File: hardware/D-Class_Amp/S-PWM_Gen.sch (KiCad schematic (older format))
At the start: 13 parts, among them U201 Opamp_Dual_Generic, U202 Comparator_Dual_Generic

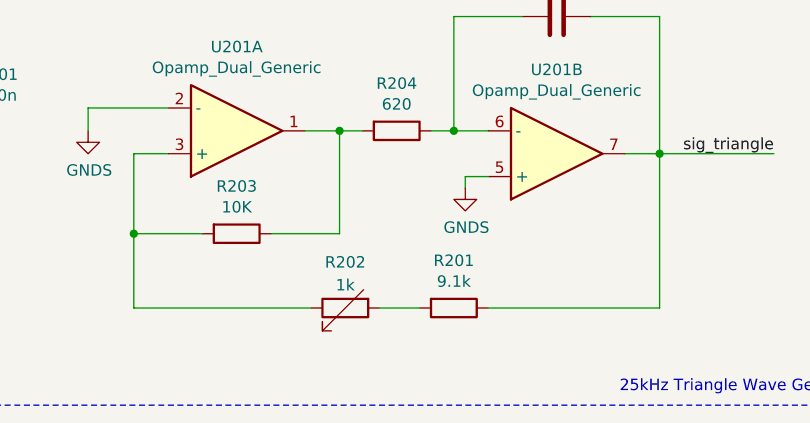
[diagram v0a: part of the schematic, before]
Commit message: update potentiometer, add footprints
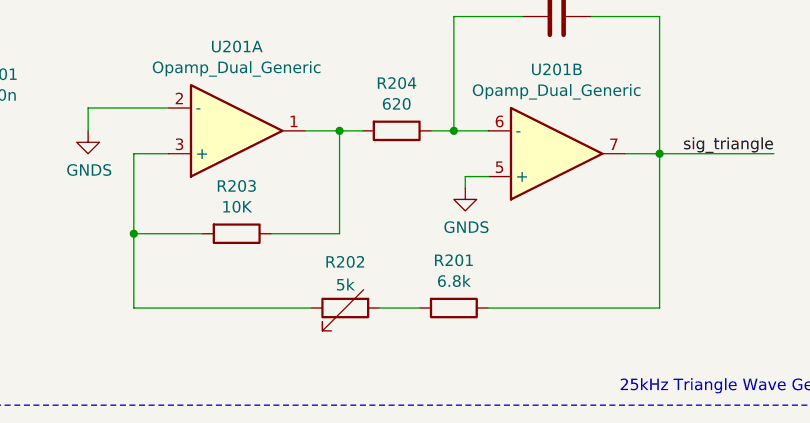
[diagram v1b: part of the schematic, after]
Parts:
- C201, C202, C203, C204, C205, R203, R204, R205, R206: footprint (none) -> Resistor_SMD:R_0805_2012Metric_Pad1.20x1.40mm_HandSolder
- R201: value 9.1k -> 6.8k; footprint (none) -> Resistor_SMD:R_0805_2012Metric_Pad1.20x1.40mm_HandSolder
- R202: value 1k -> 5k; footprint (none) -> Potentiometer_THT:Potentiometer_Vishay_T73YP_Vertical
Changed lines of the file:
@@
 F 0 "C203" V 4123 1325 50  0000 C CNN
 F 1 "15n 16V" V 4214 1325 50  0000 C CNN
-F 2 "" H 4413 1175 50  0001 C CNN
+F 2 "Resistor_SMD:R_0805_2012Metric_Pad1.20x1.40mm_HandSolder" H 4413 1175 50  0001 C CNN
 F 3 "~" H 4375 1325 50  0001 C CNN
 	1    4375 1325
@@
 F 0 "R203" V 2768 2275 50  0000 C CNN
 F 1 "10K" V 2859 2275 50  0000 C CNN
-F 2 "" V 2905 2275 50  0001 C CNN
+F 2 "Resistor_SMD:R_0805_2012Metric_Pad1.20x1.40mm_HandSolder" V 2905 2275 50  0001 C CNN
 F 3 "~" H 2975 2275 50  0001 C CNN
 	1    2975 2275
@@
 F 0 "R204" V 3468 1825 50  0000 C CNN
 F 1 "620" V 3559 1825 50  0000 C CNN
-F 2 "" V 3605 1825 50  0001 C CNN
+F 2 "Resistor_SMD:R_0805_2012Metric_Pad1.20x1.40mm_HandSolder" V 3605 1825 50  0001 C CNN
 F 3 "~" H 3675 1825 50  0001 C CNN
 	1    3675 1825
@@
 	4675 1925 4825 1925
 $Comp
-L power:GNDS #PWR?
+L power:GNDS #PWR0122
 U 1 1 61064912
 P 2325 1825
-F 0 "#PWR?" H 2325 1575 50  0001 C CNN
+F 0 "#PWR0122" H 2325 1575 50  0001 C CNN
 F 1 "GNDS" H 2330 1652 50  0000 C CNN
 F 2 "" H 2325 1825 50  0001 C CNN
@@
 	2325 1725 2325 1825
 $Comp
-L power:GNDS #PWR?
+L power:GNDS #PWR0123
 U 1 1 61065BCC
 P 3975 2075
-F 0 "#PWR?" H 3975 1825 50  0001 C CNN
+F 0 "#PWR0123" H 3975 1825 50  0001 C CNN
 F 1 "GNDS" H 3980 1902 50  0000 C CNN
 F 2 "" H 3975 2075 50  0001 C CNN
@@
 F 0 "C201" H 1840 1671 50  0000 L CNN
 F 1 "100n" H 1840 1580 50  0000 L CNN
-F 2 "" H 1763 1475 50  0001 C CNN
+F 2 "Resistor_SMD:R_0805_2012Metric_Pad1.20x1.40mm_HandSolder" H 1763 1475 50  0001 C CNN
 F 3 "~" H 1725 1625 50  0001 C CNN
 	1    1725 1625
@@
 	1025 1425 1075 1425
 $Comp
-L power:+5V #PWR?
+L power:+5V #PWR0124
 U 1 1 610CCDDC
 P 1725 1325
-F 0 "#PWR?" H 1725 1175 50  0001 C CNN
+F 0 "#PWR0124" H 1725 1175 50  0001 C CNN
 F 1 "+5V" H 1740 1498 50  0000 C CNN
 F 2 "" H 1725 1325 50  0001 C CNN
@@
 Connection ~ 1725 1425
 $Comp
-L power:GNDS #PWR?
+L power:GNDS #PWR0125
 U 1 1 610B700C
 P 1725 1775
-F 0 "#PWR?" H 1725 1525 50  0001 C CNN
+F 0 "#PWR0125" H 1725 1525 50  0001 C CNN
 F 1 "GNDS" H 1730 1602 50  0000 C CNN
 F 2 "" H 1725 1775 50  0001 C CNN
@@
 $EndComp
 $Comp
-L power:GNDS #PWR?
+L power:GNDS #PWR0126
 U 1 1 610B6C70
 P 1025 1775
-F 0 "#PWR?" H 1025 1525 50  0001 C CNN
+F 0 "#PWR0126" H 1025 1525 50  0001 C CNN
 F 1 "GNDS" H 1030 1602 50  0000 C CNN
 F 2 "" H 1025 1775 50  0001 C CNN
@@
 F 0 "C204" H 7765 1671 50  0000 L CNN
 F 1 "100n" H 7765 1580 50  0000 L CNN
-F 2 "" H 7688 1475 50  0001 C CNN
+F 2 "Resistor_SMD:R_0805_2012Metric_Pad1.20x1.40mm_HandSolder" H 7688 1475 50  0001 C CNN
 F 3 "~" H 7650 1625 50  0001 C CNN
 	1    7650 1625
@@
 	6950 1425 7000 1425
 $Comp
-L power:+5V #PWR?
+L power:+5V #PWR0127
 U 1 1 610E9B57
 P 7650 1325
-F 0 "#PWR?" H 7650 1175 50  0001 C CNN
+F 0 "#PWR0127" H 7650 1175 50  0001 C CNN
 F 1 "+5V" H 7665 1498 50  0000 C CNN
 F 2 "" H 7650 1325 50  0001 C CNN
@@
 Connection ~ 7650 1425
 $Comp
-L power:GNDS #PWR?
+L power:GNDS #PWR0128
 U 1 1 610E9B63
 P 7650 1775
-F 0 "#PWR?" H 7650 1525 50  0001 C CNN
+F 0 "#PWR0128" H 7650 1525 50  0001 C CNN
 F 1 "GNDS" H 7655 1602 50  0000 C CNN
 F 2 "" H 7650 1775 50  0001 C CNN
@@
 $EndComp
 $Comp
-L power:GNDS #PWR?
+L power:GNDS #PWR0129
 U 1 1 610E9B6D
 P 6950 1775
-F 0 "#PWR?" H 6950 1525 50  0001 C CNN
+F 0 "#PWR0129" H 6950 1525 50  0001 C CNN
 F 1 "GNDS" H 6955 1602 50  0000 C CNN
 F 2 "" H 6950 1775 50  0001 C CNN
@@
 F 0 "R205" H 9420 1171 50  0000 L CNN
 F 1 "10k" H 9420 1080 50  0000 L CNN
-F 2 "" V 9280 1125 50  0001 C CNN
+F 2 "Resistor_SMD:R_0805_2012Metric_Pad1.20x1.40mm_HandSolder" V 9280 1125 50  0001 C CNN
 F 3 "~" H 9350 1125 50  0001 C CNN
 	1    9350 1125
@@
 	9350 1375 9600 1375
 $Comp
-L power:+5V #PWR?
+L power:+5V #PWR0130
 U 1 1 61133A73
 P 9350 875
-F 0 "#PWR?" H 9350 725 50  0001 C CNN
+F 0 "#PWR0130" H 9350 725 50  0001 C CNN
 F 1 "+5V" H 9365 1048 50  0000 C CNN
 F 2 "" H 9350 875 50  0001 C CNN
@@
 F 0 "R206" H 9420 2171 50  0000 L CNN
 F 1 "10k" H 9420 2080 50  0000 L CNN
-F 2 "" V 9280 2125 50  0001 C CNN
+F 2 "Resistor_SMD:R_0805_2012Metric_Pad1.20x1.40mm_HandSolder" V 9280 2125 50  0001 C CNN
 F 3 "~" H 9350 2125 50  0001 C CNN
 	1    9350 2125
@@
 	9350 2375 9600 2375
 $Comp
-L power:+5V #PWR?
+L power:+5V #PWR0131
 U 1 1 61138A4E
 P 9350 1875
-F 0 "#PWR?" H 9350 1725 50  0001 C CNN
+F 0 "#PWR0131" H 9350 1725 50  0001 C CNN
 F 1 "+5V" H 9365 2048 50  0000 C CNN
 F 2 "" H 9350 1875 50  0001 C CNN
@@
 	9350 1875 9350 1975
 $Comp
-L power:-5V #PWR?
+L power:-5V #PWR0132
 U 1 1 611ABBDF
 P 1025 1325
-F 0 "#PWR?" H 1025 1425 50  0001 C CNN
+F 0 "#PWR0132" H 1025 1425 50  0001 C CNN
 F 1 "-5V" H 1040 1498 50  0000 C CNN
 F 2 "" H 1025 1325 50  0001 C CNN
@@
 $EndComp
 $Comp
-L power:-5V #PWR?
+L power:-5V #PWR0133
 U 1 1 611AED99
 P 6950 1325
-F 0 "#PWR?" H 6950 1425 50  0001 C CNN
+F 0 "#PWR0133" H 6950 1425 50  0001 C CNN
 F 1 "-5V" H 6965 1498 50  0000 C CNN
 F 2 "" H 6950 1325 50  0001 C CNN
@@
 P 3925 2600
 F 0 "R201" V 3718 2600 50  0000 C CNN
-F 1 "9.1k" V 3809 2600 50  0000 C CNN
-F 2 "" V 3855 2600 50  0001 C CNN
+F 1 "6.8k" V 3809 2600 50  0000 C CNN
+F 2 "Resistor_SMD:R_0805_2012Metric_Pad1.20x1.40mm_HandSolder" V 3855 2600 50  0001 C CNN
 F 3 "~" H 3925 2600 50  0001 C CNN
 	1    3925 2600
@@
 P 3450 2600
 F 0 "R202" V 3250 2600 50  0000 C CNN
-F 1 "1k" V 3350 2600 50  0000 C CNN
-F 2 "" V 3380 2600 50  0001 C CNN
+F 1 "5k" V 3350 2600 50  0000 C CNN
+F 2 "Potentiometer_THT:Potentiometer_Vishay_T73YP_Vertical" V 3380 2600 50  0001 C CNN
 F 3 "~" H 3450 2600 50  0001 C CNN
 F 4 "CT6EP102" V 3450 2600 50  0001 C CNN "Part Number"
@@
 F 0 "C202" H 1140 1671 50  0000 L CNN
 F 1 "100n" H 1140 1580 50  0000 L CNN
-F 2 "" H 1063 1475 50  0001 C CNN
+F 2 "Resistor_SMD:R_0805_2012Metric_Pad1.20x1.40mm_HandSolder" H 1063 1475 50  0001 C CNN
 F 3 "~" H 1025 1625 50  0001 C CNN
 	1    1025 1625
@@
 F 0 "C205" H 7065 1671 50  0000 L CNN
 F 1 "100n" H 7065 1580 50  0000 L CNN
-F 2 "" H 6988 1475 50  0001 C CNN
+F 2 "Resistor_SMD:R_0805_2012Metric_Pad1.20x1.40mm_HandSolder" H 6988 1475 50  0001 C CNN
 F 3 "~" H 6950 1625 50  0001 C CNN
 	1    6950 1625

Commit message: Added input bias circuit and gain stage to input-stage schematic.
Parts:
- renumbered C203 to C501, C202 to C502, C201 to C503, C205 to C504, C204 to C505, R205 to R501, R204 to R502, R206 to R503, R203 to R504, R202 to R505, R201 to R506, U202 to U501, U201 to U502
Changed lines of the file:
@@
 $EndDescr
 $Comp
-L Device:Opamp_Dual_Generic U201
+L Device:Opamp_Dual_Generic U502
 U 1 1 6104BA3C
 P 2975 1825
-F 0 "U201" H 2975 1458 50  0000 C CNN
+F 0 "U502" H 2975 1458 50  0000 C CNN
 F 1 "Opamp_Dual_Generic" H 2975 1549 50  0000 C CNN
 F 2 "" H 2975 1825 50  0001 C CNN
@@
 $EndComp
 $Comp
-L Device:Opamp_Dual_Generic U201
+L Device:Opamp_Dual_Generic U502
 U 2 1 6104BF37
 P 4375 1925
-F 0 "U201" H 4375 1558 50  0000 C CNN
+F 0 "U502" H 4375 1558 50  0000 C CNN
 F 1 "Opamp_Dual_Generic" H 4375 1649 50  0000 C CNN
 F 2 "" H 4375 1925 50  0001 C CNN
@@
 $EndComp
 $Comp
-L Device:C C203
+L Device:C C501
 U 1 1 610546D1
 P 4375 1325
-F 0 "C203" V 4123 1325 50  0000 C CNN
+F 0 "C501" V 4123 1325 50  0000 C CNN
 F 1 "15n 16V" V 4214 1325 50  0000 C CNN
 F 2 "Resistor_SMD:R_0805_2012Metric_Pad1.20x1.40mm_HandSolder" H 4413 1175 50  0001 C CNN
@@
 $EndComp
 $Comp
-L Device:R R203
+L Device:R R504
 U 1 1 61054D4F
 P 2975 2275
-F 0 "R203" V 2768 2275 50  0000 C CNN
+F 0 "R504" V 2768 2275 50  0000 C CNN
 F 1 "10K" V 2859 2275 50  0000 C CNN
 F 2 "Resistor_SMD:R_0805_2012Metric_Pad1.20x1.40mm_HandSolder" V 2905 2275 50  0001 C CNN
@@
 $EndComp
 $Comp
-L Device:R R204
+L Device:R R502
 U 1 1 610560D6
 P 3675 1825
-F 0 "R204" V 3468 1825 50  0000 C CNN
+F 0 "R502" V 3468 1825 50  0000 C CNN
 F 1 "620" V 3559 1825 50  0000 C CNN
 F 2 "Resistor_SMD:R_0805_2012Metric_Pad1.20x1.40mm_HandSolder" V 3605 1825 50  0001 C CNN
@@
 	4675 1925 4825 1925
 $Comp
-L power:GNDS #PWR0122
+L power:GNDS #PWR0510
 U 1 1 61064912
 P 2325 1825
-F 0 "#PWR0122" H 2325 1575 50  0001 C CNN
+F 0 "#PWR0510" H 2325 1575 50  0001 C CNN
 F 1 "GNDS" H 2330 1652 50  0000 C CNN
 F 2 "" H 2325 1825 50  0001 C CNN
@@
 	2325 1725 2325 1825
 $Comp
-L power:GNDS #PWR0123
+L power:GNDS #PWR0512
 U 1 1 61065BCC
 P 3975 2075
-F 0 "#PWR0123" H 3975 1825 50  0001 C CNN
+F 0 "#PWR0512" H 3975 1825 50  0001 C CNN
 F 1 "GNDS" H 3980 1902 50  0000 C CNN
 F 2 "" H 3975 2075 50  0001 C CNN
@@
 Connection ~ 4825 1925
 $Comp
-L Device:C C201
+L Device:C C503
 U 1 1 610B8642
 P 1725 1625
-F 0 "C201" H 1840 1671 50  0000 L CNN
+F 0 "C503" H 1840 1671 50  0000 L CNN
 F 1 "100n" H 1840 1580 50  0000 L CNN
 F 2 "Resistor_SMD:R_0805_2012Metric_Pad1.20x1.40mm_HandSolder" H 1763 1475 50  0001 C CNN
@@
 $EndComp
 $Comp
-L Device:Opamp_Dual_Generic U201
+L Device:Opamp_Dual_Generic U502
 U 3 1 6104C970
 P 1375 1525
-F 0 "U201" V 675 1525 50  0000 C CNN
+F 0 "U502" V 675 1525 50  0000 C CNN
 F 1 "Opamp_Dual_Generic" V 775 1525 50  0000 C CNN
 F 2 "" H 1375 1525 50  0001 C CNN
@@
 	1025 1425 1075 1425
 $Comp
-L power:+5V #PWR0124
+L power:+5V #PWR0503
 U 1 1 610CCDDC
 P 1725 1325
-F 0 "#PWR0124" H 1725 1175 50  0001 C CNN
+F 0 "#PWR0503" H 1725 1175 50  0001 C CNN
 F 1 "+5V" H 1740 1498 50  0000 C CNN
 F 2 "" H 1725 1325 50  0001 C CNN
@@
 Connection ~ 1725 1425
 $Comp
-L power:GNDS #PWR0125
+L power:GNDS #PWR0507
 U 1 1 610B700C
 P 1725 1775
-F 0 "#PWR0125" H 1725 1525 50  0001 C CNN
+F 0 "#PWR0507" H 1725 1525 50  0001 C CNN
 F 1 "GNDS" H 1730 1602 50  0000 C CNN
 F 2 "" H 1725 1775 50  0001 C CNN
@@
 $EndComp
 $Comp
-L power:GNDS #PWR0126
+L power:GNDS #PWR0506
 U 1 1 610B6C70
 P 1025 1775
-F 0 "#PWR0126" H 1025 1525 50  0001 C CNN
+F 0 "#PWR0506" H 1025 1525 50  0001 C CNN
 F 1 "GNDS" H 1030 1602 50  0000 C CNN
 F 2 "" H 1025 1775 50  0001 C CNN
@@
 ~S-PWM
 $Comp
-L Device:Opamp_Dual_Generic U202
+L Device:Opamp_Dual_Generic U501
 U 1 1 610E84D1
 P 8750 1375
-F 0 "U202" H 8750 1008 50  0000 C CNN
+F 0 "U501" H 8750 1008 50  0000 C CNN
 F 1 "Comparator_Dual_Generic" H 8750 1099 50  0000 C CNN
 F 2 "" H 8750 1375 50  0001 C CNN
@@
 $EndComp
 $Comp
-L Device:Opamp_Dual_Generic U202
+L Device:Opamp_Dual_Generic U501
 U 2 1 610E8A2F
 P 8750 2375
-F 0 "U202" H 8750 2742 50  0000 C CNN
+F 0 "U501" H 8750 2742 50  0000 C CNN
 F 1 "Comparator_Dual_Generic" H 8750 2651 50  0000 C CNN
 F 2 "" H 8750 2375 50  0001 C CNN
@@
 $EndComp
 $Comp
-L Device:C C204
+L Device:C C505
 U 1 1 610E9B40
 P 7650 1625
-F 0 "C204" H 7765 1671 50  0000 L CNN
+F 0 "C505" H 7765 1671 50  0000 L CNN
 F 1 "100n" H 7765 1580 50  0000 L CNN
 F 2 "Resistor_SMD:R_0805_2012Metric_Pad1.20x1.40mm_HandSolder" H 7688 1475 50  0001 C CNN
@@
 $EndComp
 $Comp
-L Device:Opamp_Dual_Generic U202
+L Device:Opamp_Dual_Generic U501
 U 3 1 610E9B4A
 P 7300 1525
-F 0 "U202" V 6600 1525 50  0000 C CNN
+F 0 "U501" V 6600 1525 50  0000 C CNN
 F 1 "Comparator_Dual_Generic" V 6700 1525 50  0000 C CNN
 F 2 "" H 7300 1525 50  0001 C CNN
@@
 	6950 1425 7000 1425
 $Comp
-L power:+5V #PWR0127
+L power:+5V #PWR0505
 U 1 1 610E9B57
 P 7650 1325
-F 0 "#PWR0127" H 7650 1175 50  0001 C CNN
+F 0 "#PWR0505" H 7650 1175 50  0001 C CNN
 F 1 "+5V" H 7665 1498 50  0000 C CNN
 F 2 "" H 7650 1325 50  0001 C CNN
@@
 Connection ~ 7650 1425
 $Comp
-L power:GNDS #PWR0128
+L power:GNDS #PWR0509
 U 1 1 610E9B63
 P 7650 1775
-F 0 "#PWR0128" H 7650 1525 50  0001 C CNN
+F 0 "#PWR0509" H 7650 1525 50  0001 C CNN
 F 1 "GNDS" H 7655 1602 50  0000 C CNN
 F 2 "" H 7650 1775 50  0001 C CNN
@@
 $EndComp
 $Comp
-L power:GNDS #PWR0129
+L power:GNDS #PWR0508
 U 1 1 610E9B6D
 P 6950 1775
-F 0 "#PWR0129" H 6950 1525 50  0001 C CNN
+F 0 "#PWR0508" H 6950 1525 50  0001 C CNN
 F 1 "GNDS" H 6955 1602 50  0000 C CNN
 F 2 "" H 6950 1775 50  0001 C CNN
@@
 	9050 1375 9350 1375
 $Comp
-L Device:R R205
+L Device:R R501
 U 1 1 6112AEF0
 P 9350 1125
-F 0 "R205" H 9420 1171 50  0000 L CNN
+F 0 "R501" H 9420 1171 50  0000 L CNN
 F 1 "10k" H 9420 1080 50  0000 L CNN
 F 2 "Resistor_SMD:R_0805_2012Metric_Pad1.20x1.40mm_HandSolder" V 9280 1125 50  0001 C CNN
@@
 	9350 1375 9600 1375
 $Comp
-L power:+5V #PWR0130
+L power:+5V #PWR0501
 U 1 1 61133A73
 P 9350 875
-F 0 "#PWR0130" H 9350 725 50  0001 C CNN
+F 0 "#PWR0501" H 9350 725 50  0001 C CNN
 F 1 "+5V" H 9365 1048 50  0000 C CNN
 F 2 "" H 9350 875 50  0001 C CNN
@@
 	9050 2375 9350 2375
 $Comp
-L Device:R R206
+L Device:R R503
 U 1 1 61138A41
 P 9350 2125
-F 0 "R206" H 9420 2171 50  0000 L CNN
+F 0 "R503" H 9420 2171 50  0000 L CNN
 F 1 "10k" H 9420 2080 50  0000 L CNN
 F 2 "Resistor_SMD:R_0805_2012Metric_Pad1.20x1.40mm_HandSolder" V 9280 2125 50  0001 C CNN
@@
 	9350 2375 9600 2375
 $Comp
-L power:+5V #PWR0131
+L power:+5V #PWR0511
 U 1 1 61138A4E
 P 9350 1875
-F 0 "#PWR0131" H 9350 1725 50  0001 C CNN
+F 0 "#PWR0511" H 9350 1725 50  0001 C CNN
 F 1 "+5V" H 9365 2048 50  0000 C CNN
 F 2 "" H 9350 1875 50  0001 C CNN
@@
 	9350 1875 9350 1975
 $Comp
-L power:-5V #PWR0132
+L power:-5V #PWR0502
 U 1 1 611ABBDF
 P 1025 1325
-F 0 "#PWR0132" H 1025 1425 50  0001 C CNN
+F 0 "#PWR0502" H 1025 1425 50  0001 C CNN
 F 1 "-5V" H 1040 1498 50  0000 C CNN
 F 2 "" H 1025 1325 50  0001 C CNN
@@
 $EndComp
 $Comp
-L power:-5V #PWR0133
+L power:-5V #PWR0504
 U 1 1 611AED99
 P 6950 1325
-F 0 "#PWR0133" H 6950 1425 50  0001 C CNN
+F 0 "#PWR0504" H 6950 1425 50  0001 C CNN
 F 1 "-5V" H 6965 1498 50  0000 C CNN
 F 2 "" H 6950 1325 50  0001 C CNN
@@
 	6300 3025 6300 475
 $Comp
-L Device:R R201
+L Device:R R506
 U 1 1 61055E03
 P 3925 2600
-F 0 "R201" V 3718 2600 50  0000 C CNN
+F 0 "R506" V 3718 2600 50  0000 C CNN
 F 1 "6.8k" V 3809 2600 50  0000 C CNN
 F 2 "Resistor_SMD:R_0805_2012Metric_Pad1.20x1.40mm_HandSolder" V 3855 2600 50  0001 C CNN
@@
 $EndComp
 $Comp
-L Device:R_Variable R202
+L Device:R_Variable R505
 U 1 1 6105EC41
 P 3450 2600
-F 0 "R202" V 3250 2600 50  0000 C CNN
+F 0 "R505" V 3250 2600 50  0000 C CNN
 F 1 "5k" V 3350 2600 50  0000 C CNN
 F 2 "Potentiometer_THT:Potentiometer_Vishay_T73YP_Vertical" V 3380 2600 50  0001 C CNN
@@
 	4825 1925 4825 2600
 $Comp
-L Device:C C202
+L Device:C C502
 U 1 1 61084C95
 P 1025 1625
-F 0 "C202" H 1140 1671 50  0000 L CNN
+F 0 "C502" H 1140 1671 50  0000 L CNN
 F 1 "100n" H 1140 1580 50  0000 L CNN
 F 2 "Resistor_SMD:R_0805_2012Metric_Pad1.20x1.40mm_HandSolder" H 1063 1475 50  0001 C CNN
@@
 Connection ~ 1025 1425
 $Comp
-L Device:C C205
+L Device:C C504
 U 1 1 61090BA0
 P 6950 1625
-F 0 "C205" H 7065 1671 50  0000 L CNN
+F 0 "C504" H 7065 1671 50  0000 L CNN
 F 1 "100n" H 7065 1580 50  0000 L CNN
 F 2 "Resistor_SMD:R_0805_2012Metric_Pad1.20x1.40mm_HandSolder" H 6988 1475 50  0001 C CNN

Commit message: added footprints for opamp
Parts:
- removed C502, C504: 100n, Resistor_SMD:R_0805_2012Metric_Pad1.20x1.40mm_HandSolder, symbol Device:C
- U501: renamed from U502; value Opamp_Dual_Generic -> MAX4016; footprint (none) -> Package_SO:SOIC-8_3.9x4.9mm_P1.27mm
- renumbered C503 to C501, C501 to C502, C505 to C503, R504 to R501, R505 to R502, R502 to R503, R506 to R504, R501 to R505, R503 to R506, U501 to U502
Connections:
- net labels added: +2V5
- net labels removed: -5V
- wire segments 44 -> 42
